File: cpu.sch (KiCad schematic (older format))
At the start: 30 parts

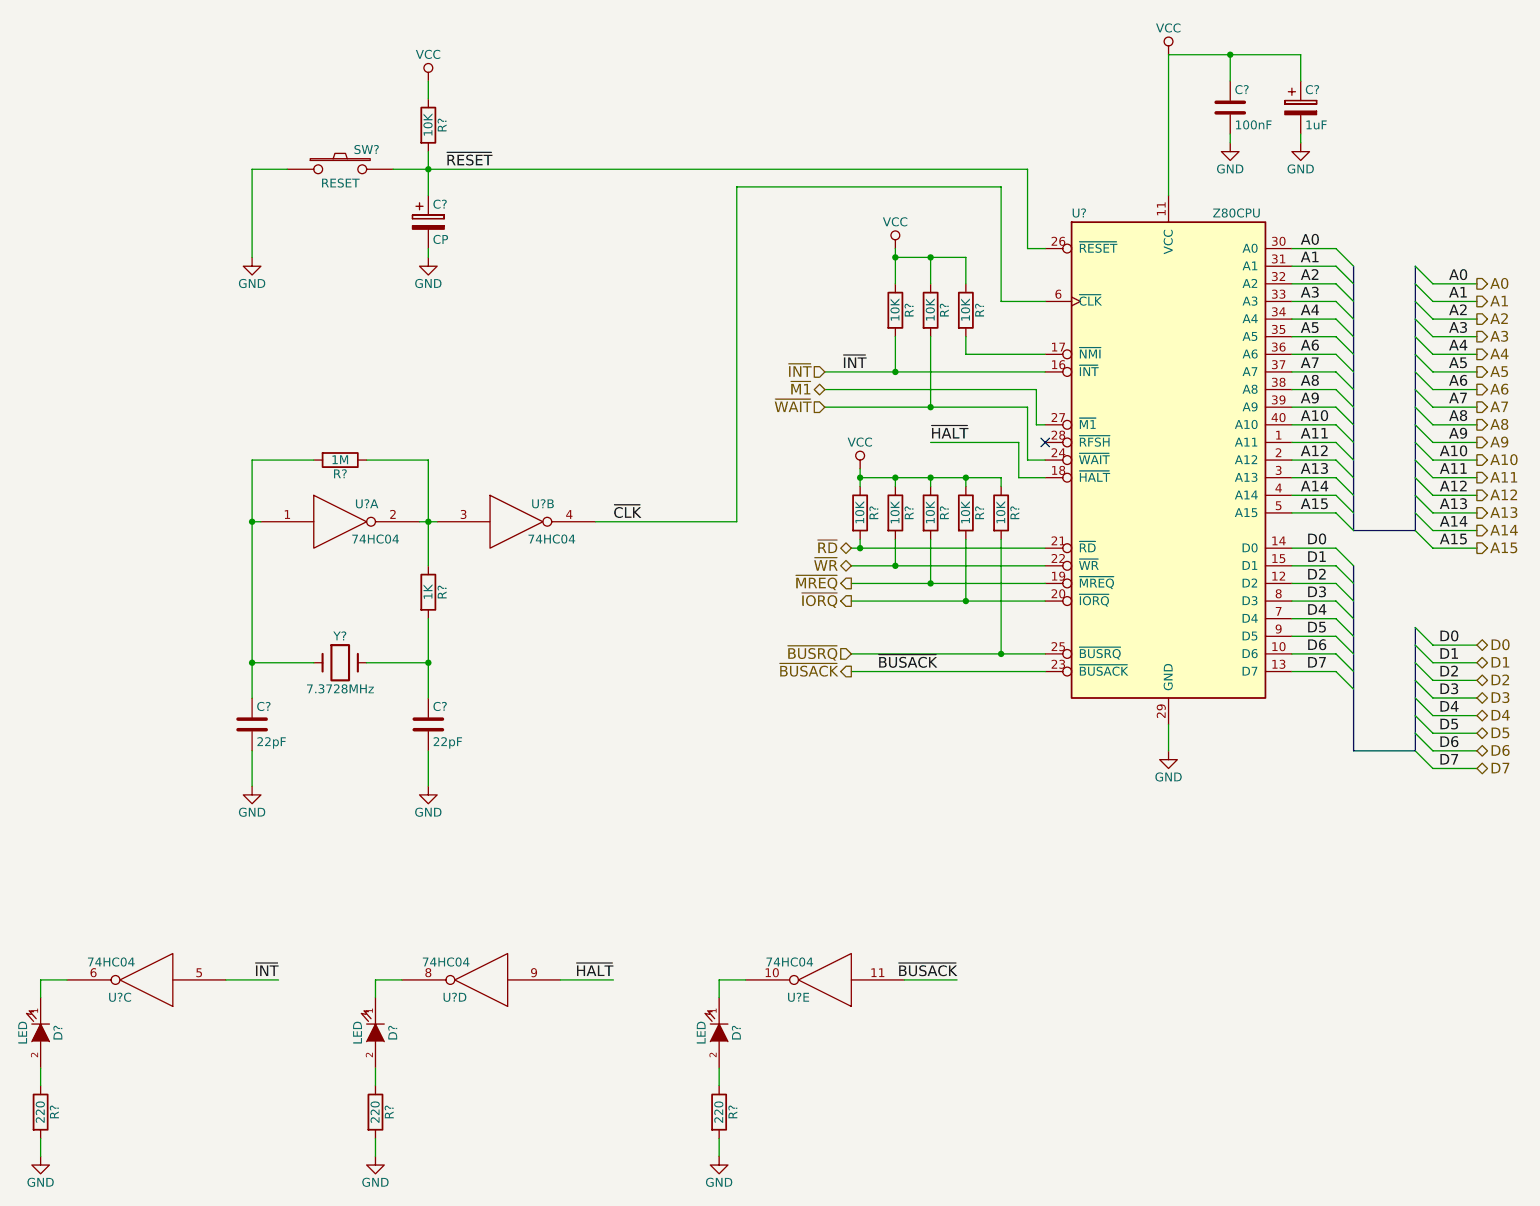
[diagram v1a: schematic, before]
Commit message: More WIP added hierarchical sheets for bus
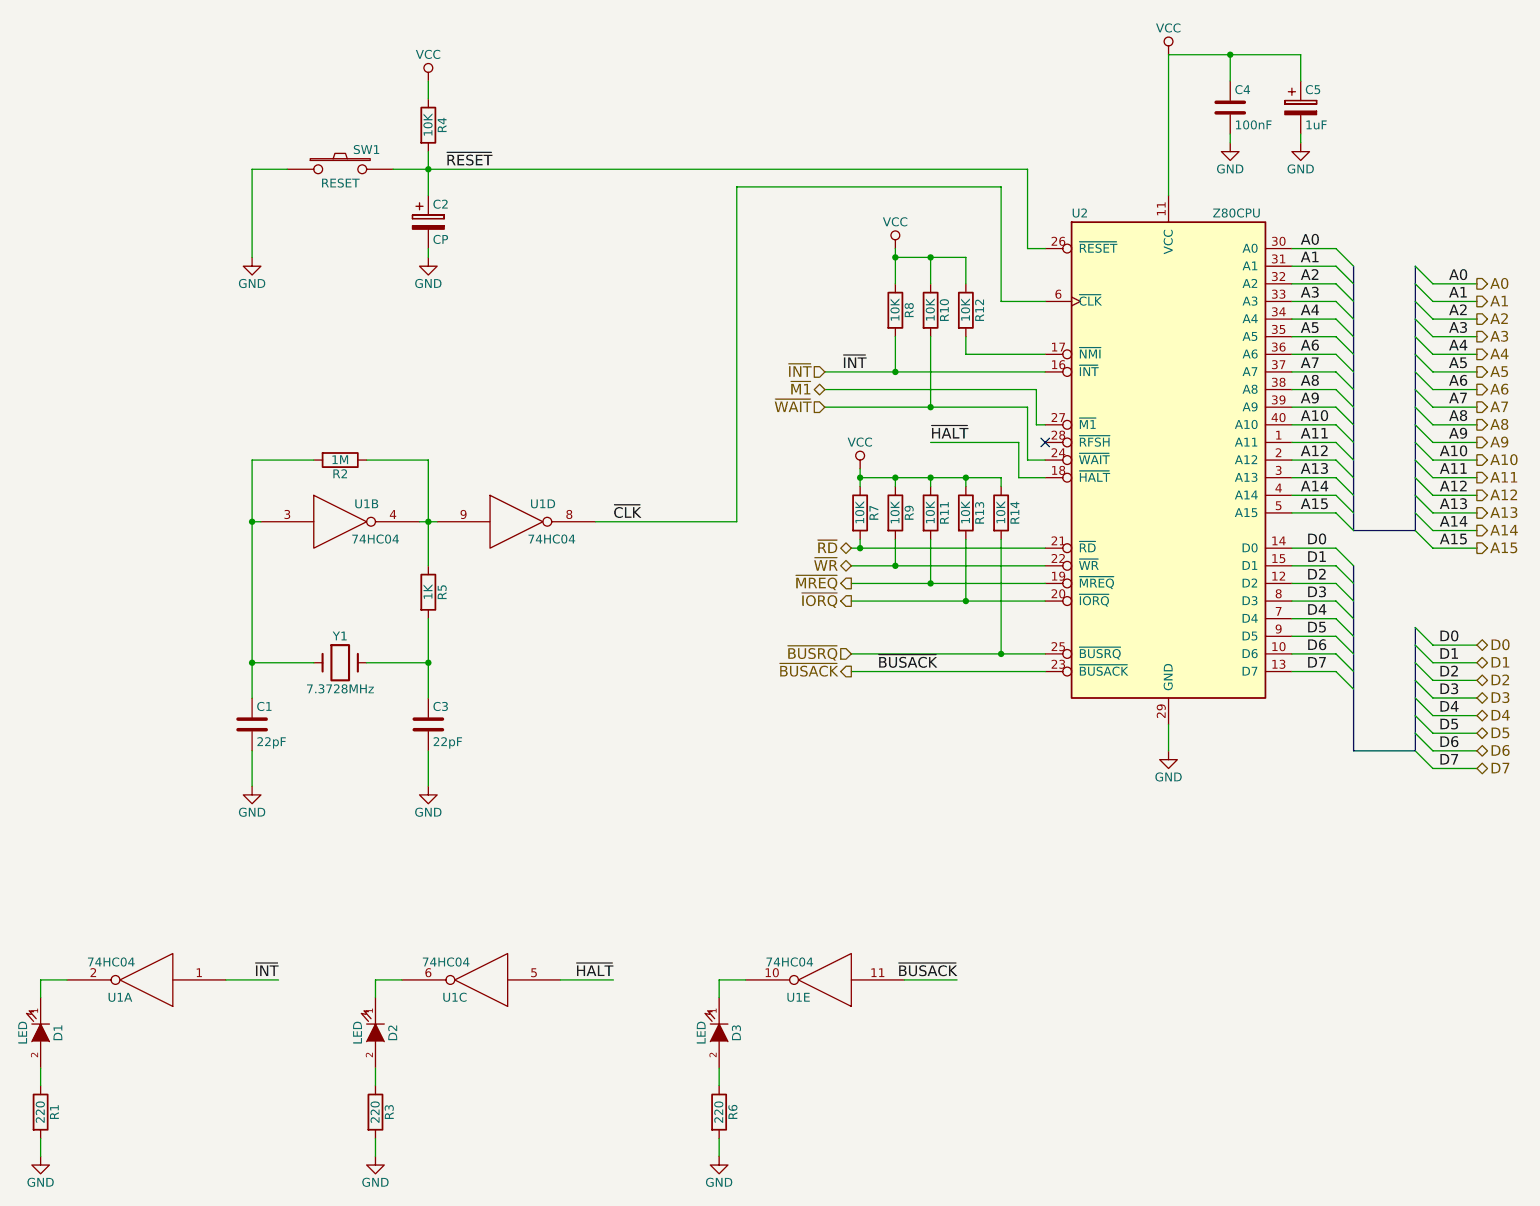
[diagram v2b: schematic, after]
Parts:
- C1, C3, C4: renamed from C?; footprint (none) -> Capacitors_SMD:C_0805_HandSoldering
- C2, C5: renamed from C?; footprint (none) -> Capacitors_ThroughHole:C_Radial_D6.3_L11.2_P2.5
- D1, D2, D3: renamed from D?; footprint (none) -> LEDs:LED-3MM
- R1, R10, R11, R12, R13, R14, R2, R3, R4, R5, R6, R7, R8, R9: renamed from R?; footprint (none) -> Resistors_SMD:R_0805_HandSoldering
- SW1: renamed from SW?; footprint (none) -> Buttons_Switches_SMD:SW_SPST_B3SL-1002P
- U1: renamed from U?; footprint (none) -> Housings_DIP:DIP-14_W7.62mm_LongPads
- U2: renamed from U?; footprint (none) -> Housings_DIP:DIP-40_W25.4mm_LongPads
- Y1: renamed from Y?; footprint (none) -> Crystals:Crystal_HC49-U_Vertical
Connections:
- net ~CLK: now also U1.8; no longer U1.4
- net ~HALT: now also U1.5; no longer U1.9
- net ~INT: now also U1.1; no longer U1.5
- net at R2.1, R5.1: now also U1.4, U1.9; no longer U1.2, U1.3
- net at C1.1, R2.2, Y1.1: now also U1.3; no longer U1.1
- net at D2.1 (K): now also U1.6; no longer U1.8
- net at D1.1 (K): now also U1.2; no longer U1.6

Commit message: Added seperate power pin slots to stop inserting cards backwards
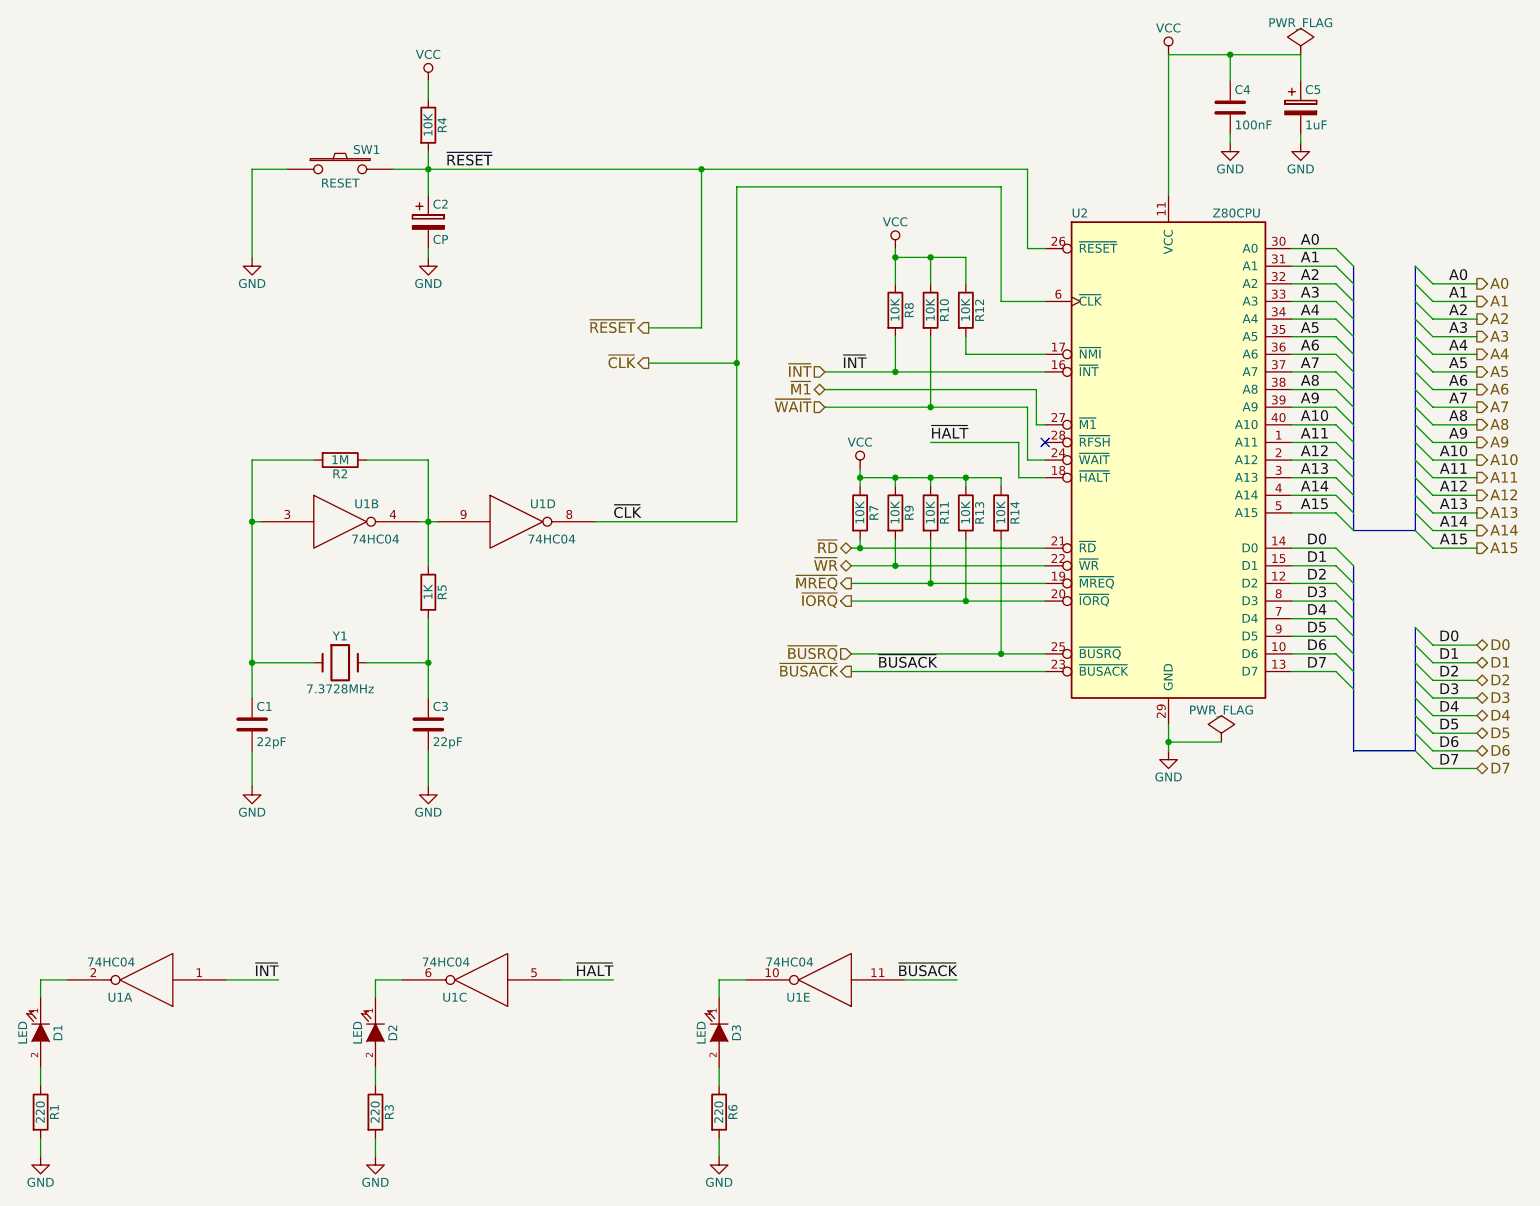
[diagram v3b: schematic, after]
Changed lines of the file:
@@
 	9650 4700 9300 4700
 $Comp
-L VCC #PWR9
+L VCC #PWR01
 U 1 1 577A5457
 P 6500 3100
-F 0 "#PWR9" H 6500 2950 50  0001 C CNN
+F 0 "#PWR01" H 6500 2950 50  0001 C CNN
 F 1 "VCC" H 6500 3250 50  0000 C CNN
 F 2 "" H 6500 3100 50  0000 C CNN
@@
 $EndComp
 $Comp
-L VCC #PWR10
+L VCC #PWR02
 U 1 1 577A54A8
 P 6700 1850
-F 0 "#PWR10" H 6700 1700 50  0001 C CNN
+F 0 "#PWR02" H 6700 1700 50  0001 C CNN
 F 1 "VCC" H 6700 2000 50  0000 C CNN
 F 2 "" H 6700 1850 50  0000 C CNN
@@
 	8250 1550 8250 750
 $Comp
-L VCC #PWR11
+L VCC #PWR03
 U 1 1 577A54FB
 P 8250 750
-F 0 "#PWR11" H 8250 600 50  0001 C CNN
+F 0 "#PWR03" H 8250 600 50  0001 C CNN
 F 1 "VCC" H 8250 900 50  0000 C CNN
 F 2 "" H 8250 750 50  0000 C CNN
@@
 	8250 4550 8250 4700
 $Comp
-L GND #PWR12
+L GND #PWR04
 U 1 1 577A554F
 P 8250 4700
-F 0 "#PWR12" H 8250 4450 50  0001 C CNN
+F 0 "#PWR04" H 8250 4450 50  0001 C CNN
 F 1 "GND" H 8250 4550 50  0000 C CNN
 F 2 "" H 8250 4700 50  0000 C CNN
@@
 	4050 4700 4050 4900
 $Comp
-L GND #PWR3
+L GND #PWR05
 U 1 1 577B2CBE
 P 3050 4900
-F 0 "#PWR3" H 3050 4650 50  0001 C CNN
+F 0 "#PWR05" H 3050 4650 50  0001 C CNN
 F 1 "GND" H 3050 4750 50  0000 C CNN
 F 2 "" H 3050 4900 50  0000 C CNN
@@
 $EndComp
 $Comp
-L GND #PWR7
+L GND #PWR06
 U 1 1 577B2D0B
 P 4050 4900
-F 0 "#PWR7" H 4050 4650 50  0001 C CNN
+F 0 "#PWR06" H 4050 4650 50  0001 C CNN
 F 1 "GND" H 4050 4750 50  0000 C CNN
 F 2 "" H 4050 4900 50  0000 C CNN
@@
 $EndComp
 $Comp
-L GND #PWR4
+L GND #PWR07
 U 1 1 577B377E
 P 3750 7000
-F 0 "#PWR4" H 3750 6750 50  0001 C CNN
+F 0 "#PWR07" H 3750 6750 50  0001 C CNN
 F 1 "GND" H 3750 6850 50  0000 C CNN
 F 2 "" H 3750 7000 50  0000 C CNN
@@
 	3050 1400 3050 1900
 $Comp
-L GND #PWR2
+L GND #PWR08
 U 1 1 577B455D
 P 3050 1900
-F 0 "#PWR2" H 3050 1650 50  0001 C CNN
+F 0 "#PWR08" H 3050 1650 50  0001 C CNN
 F 1 "GND" H 3050 1750 50  0000 C CNN
 F 2 "" H 3050 1900 50  0000 C CNN
@@
 	4050 1850 4050 1900
 $Comp
-L GND #PWR6
+L GND #PWR09
 U 1 1 577B48FE
 P 4050 1900
-F 0 "#PWR6" H 4050 1650 50  0001 C CNN
+F 0 "#PWR09" H 4050 1650 50  0001 C CNN
 F 1 "GND" H 4050 1750 50  0000 C CNN
 F 2 "" H 4050 1900 50  0000 C CNN
@@
 $EndComp
 $Comp
-L GND #PWR1
+L GND #PWR010
 U 1 1 577B4B0C
 P 1850 7000
-F 0 "#PWR1" H 1850 6750 50  0001 C CNN
+F 0 "#PWR010" H 1850 6750 50  0001 C CNN
 F 1 "GND" H 1850 6850 50  0000 C CNN
 F 2 "" H 1850 7000 50  0000 C CNN
@@
 $EndComp
 $Comp
-L VCC #PWR5
+L VCC #PWR011
 U 1 1 577B4D04
 P 4050 900
-F 0 "#PWR5" H 4050 750 50  0001 C CNN
+F 0 "#PWR011" H 4050 750 50  0001 C CNN
 F 1 "VCC" H 4050 1050 50  0000 C CNN
 F 2 "" H 4050 900 50  0000 C CNN
@@
 $EndComp
 $Comp
-L GND #PWR8
+L GND #PWR012
 U 1 1 577B52BF
 P 5700 7000
-F 0 "#PWR8" H 5700 6750 50  0001 C CNN
+F 0 "#PWR012" H 5700 6750 50  0001 C CNN
 F 1 "GND" H 5700 6850 50  0000 C CNN
 F 2 "" H 5700 7000 50  0000 C CNN
@@
 Connection ~ 8600 750
 $Comp
-L GND #PWR13
+L GND #PWR013
 U 1 1 577B59DE
 P 8600 1250
-F 0 "#PWR13" H 8600 1000 50  0001 C CNN
+F 0 "#PWR013" H 8600 1000 50  0001 C CNN
 F 1 "GND" H 8600 1100 50  0000 C CNN
 F 2 "" H 8600 1250 50  0000 C CNN
@@
 $EndComp
 $Comp
-L GND #PWR14
+L GND #PWR014
 U 1 1 577B5A43
 P 9000 1250
-F 0 "#PWR14" H 9000 1000 50  0001 C CNN
+F 0 "#PWR014" H 9000 1000 50  0001 C CNN
 F 1 "GND" H 9000 1100 50  0000 C CNN
 F 2 "" H 9000 1250 50  0000 C CNN
@@
 Wire Wire Line
 	9000 1200 9000 1250
+Wire Wire Line
+	5800 2500 5300 2500
+Connection ~ 5800 2500
+Text HLabel 5300 2500 0    60   Output ~ 0
+~CLK
+Wire Wire Line
+	5600 1400 5600 2300
+Wire Wire Line
+	5600 2300 5300 2300
+Connection ~ 5600 1400
+Text HLabel 5300 2300 0    60   Output ~ 0
+~RESET
+$Comp
+L PWR_FLAG #FLG015
+U 1 1 5780650C
+P 9000 750
+F 0 "#FLG015" H 9000 845 50  0001 C CNN
+F 1 "PWR_FLAG" H 9000 930 50  0000 C CNN
+F 2 "" H 9000 750 50  0000 C CNN
+F 3 "" H 9000 750 50  0000 C CNN
+	1    9000 750
+	1    0    0    -1
+$EndComp
+$Comp
+L PWR_FLAG #FLG016
+U 1 1 57806779
+P 8550 4650
+F 0 "#FLG016" H 8550 4745 50  0001 C CNN
+F 1 "PWR_FLAG" H 8550 4830 50  0000 C CNN
+F 2 "" H 8550 4650 50  0000 C CNN
+F 3 "" H 8550 4650 50  0000 C CNN
+	1    8550 4650
+	1    0    0    -1
+$EndComp
+Wire Wire Line
+	8550 4650 8250 4650
+Connection ~ 8250 4650
 $EndSCHEMATC

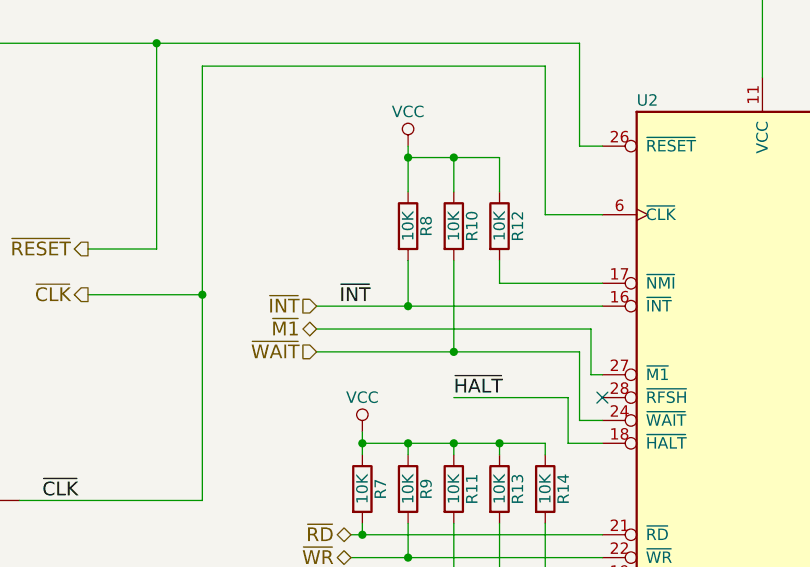
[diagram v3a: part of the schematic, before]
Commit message: More card slot clean up. Added NMI signal for DMA
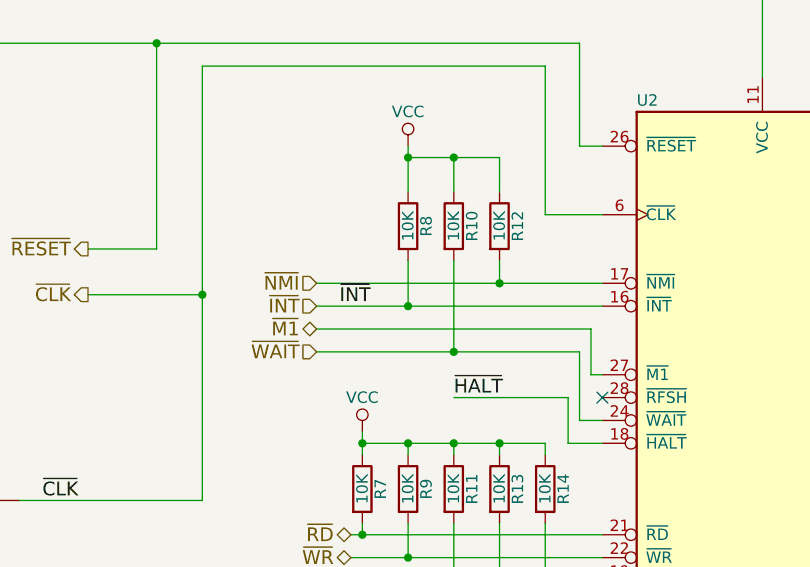
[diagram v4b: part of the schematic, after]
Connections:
- net ~NMI: now reaches R12.2, U2.17 (~NMI~)
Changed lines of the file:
@@
 	7100 2350 7100 2450
 Wire Wire Line
-	7100 2450 7550 2450
+	6300 2450 7550 2450
 Connection ~ 6700 1900
 Text HLabel 6300 2750 0    60   Input ~ 0
@@
 	8550 4650 8250 4650
 Connection ~ 8250 4650
+Connection ~ 7100 2450
+Text HLabel 6300 2450 0    60   Input ~ 0
+~NMI
 $EndSCHEMATC
